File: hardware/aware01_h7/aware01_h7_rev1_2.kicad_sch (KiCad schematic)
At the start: 60 parts, among them J1 Conn_01x06_Pin, J2 Conn_01x03_Pin, SW1 SW_Push, U1 STM32H7B0ZBTx, U2 IS45S16800F-7TLA2, Y1 WE-XTAL 24.0MHz 50ppm

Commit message: update to rev 1.2
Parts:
- C1, C2: Manufacturer_Name KEMET -> KEMET
- C14, C7: Manufacturer_Name Samsung Electro-Mechanics -> Samsung Electro-Mechanics
- R40, R41, R42, R43, R44, R45, R46, R47, R48, R49, R50, R51, R52, R53, R54, R55, R56, R57, R58, R59, R60, R61, R62, R63, R64, R65, R66, R67, R68, R69, R70, R71, R72, R73, R74, R75, R76, R77: value 10 -> 33; footprint (none) -> Resistor_SMD:R_0603_1608Metric_Pad0.98x0.95mm_HandSolder; Manufacturer_Name (none) -> Susumu; Manufacturer_Part_Number (none) -> RR0510R-330-D; Mouser Part Number (none) -> 754-RR0510R-330D
- SW1: Manufacturer_Part_Number TS04-66-43-BK-100-SMT -> TS04-66-43-BK-100-SMT
- U1: Manufacturer_Part_Number STM32H7B0ZBT6 -> STM32H7B0ZBT6; Mouser Part Number 511-STM32H7B0ZBT6 -> 511-STM32H7B0ZBT6
- U2: Manufacturer_Name ISSI -> ISSI; Mouser Part Number 870-IS45S16800F7TLA2 -> 870-IS45S16800F7TLA2
- Y1: Mouser Part Number 710-830064703 -> 710-830064703

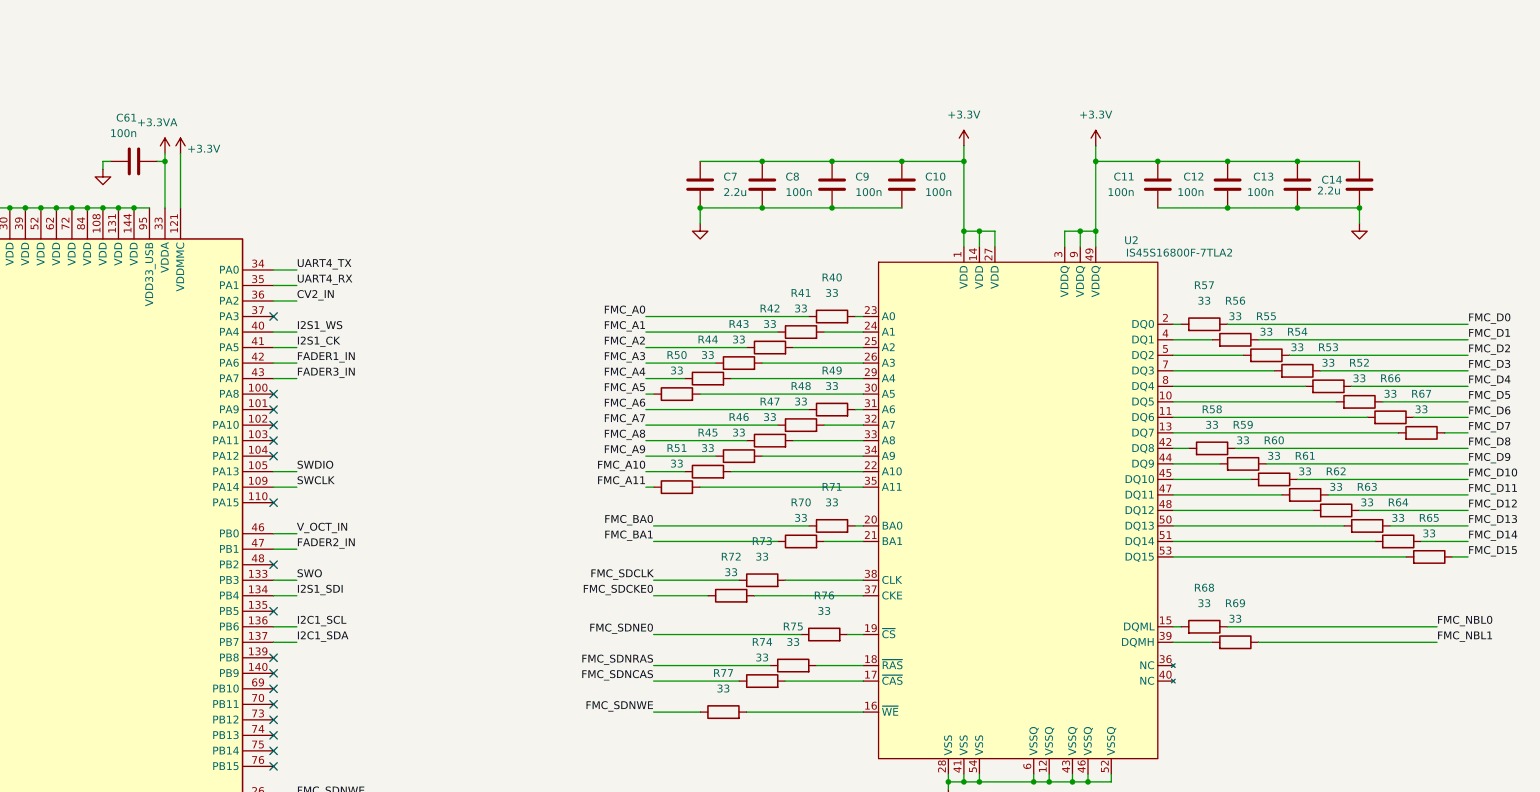
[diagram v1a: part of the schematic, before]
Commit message: rework layout and insert eletrolytic caps for gainstages
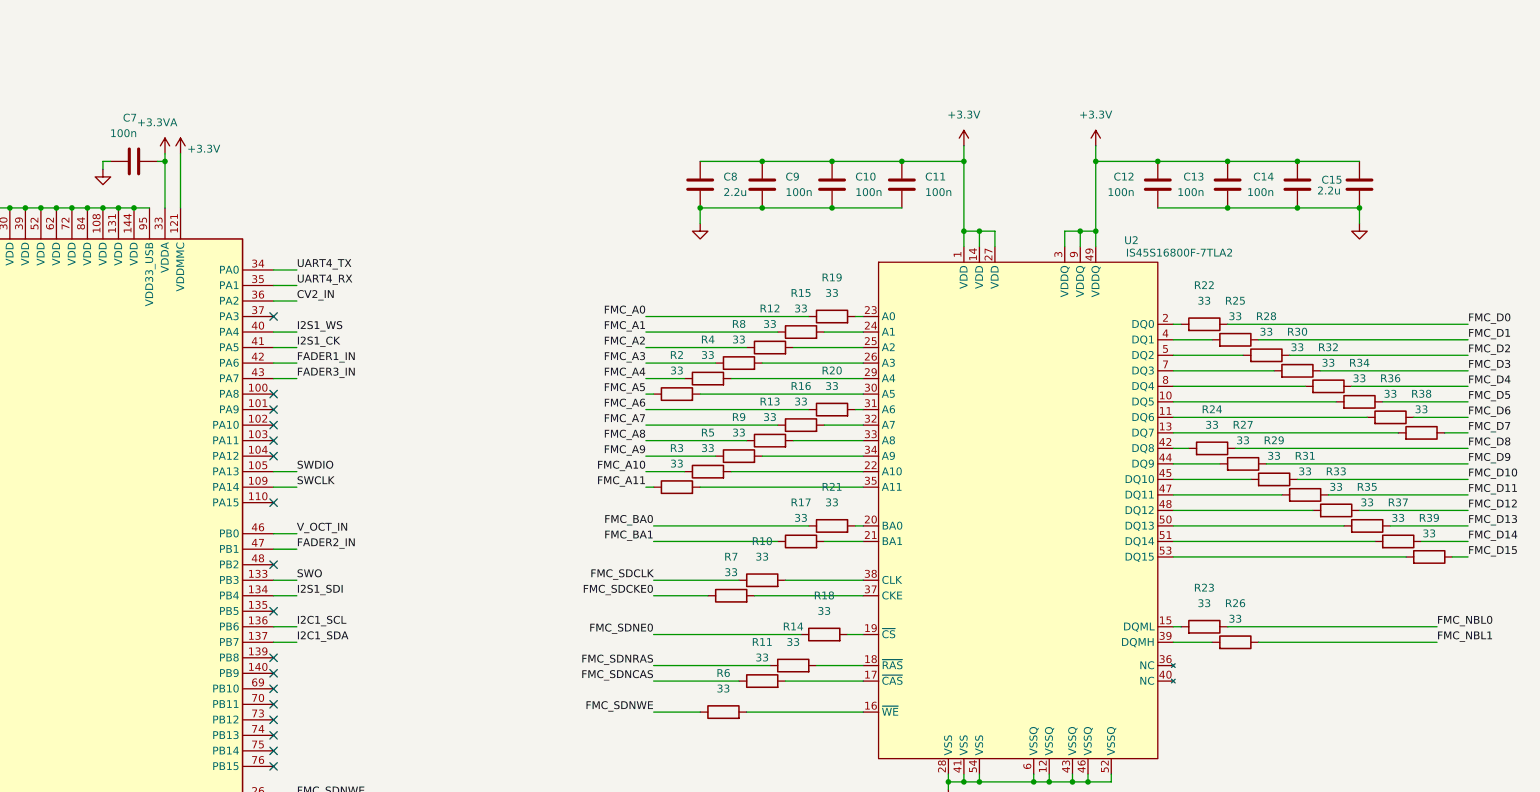
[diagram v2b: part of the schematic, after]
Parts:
- R10: renamed from R73; footprint Resistor_SMD:R_0603_1608Metric_Pad0.98x0.95mm_HandSolder -> Resistor_SMD:R_0402_1005Metric_Pad0.72x0.64mm_HandSolder
- R11: renamed from R74; footprint Resistor_SMD:R_0603_1608Metric_Pad0.98x0.95mm_HandSolder -> Resistor_SMD:R_0402_1005Metric_Pad0.72x0.64mm_HandSolder
- R12: renamed from R42; footprint Resistor_SMD:R_0603_1608Metric_Pad0.98x0.95mm_HandSolder -> Resistor_SMD:R_0402_1005Metric_Pad0.72x0.64mm_HandSolder
- R13: renamed from R47; footprint Resistor_SMD:R_0603_1608Metric_Pad0.98x0.95mm_HandSolder -> Resistor_SMD:R_0402_1005Metric_Pad0.72x0.64mm_HandSolder
- R14: renamed from R75; footprint Resistor_SMD:R_0603_1608Metric_Pad0.98x0.95mm_HandSolder -> Resistor_SMD:R_0402_1005Metric_Pad0.72x0.64mm_HandSolder
- R15: renamed from R41; footprint Resistor_SMD:R_0603_1608Metric_Pad0.98x0.95mm_HandSolder -> Resistor_SMD:R_0402_1005Metric_Pad0.72x0.64mm_HandSolder
- R16: renamed from R48; footprint Resistor_SMD:R_0603_1608Metric_Pad0.98x0.95mm_HandSolder -> Resistor_SMD:R_0402_1005Metric_Pad0.72x0.64mm_HandSolder
- R17: renamed from R70; footprint Resistor_SMD:R_0603_1608Metric_Pad0.98x0.95mm_HandSolder -> Resistor_SMD:R_0402_1005Metric_Pad0.72x0.64mm_HandSolder
- R18: renamed from R76; footprint Resistor_SMD:R_0603_1608Metric_Pad0.98x0.95mm_HandSolder -> Resistor_SMD:R_0402_1005Metric_Pad0.72x0.64mm_HandSolder
- R19: renamed from R40; footprint Resistor_SMD:R_0603_1608Metric_Pad0.98x0.95mm_HandSolder -> Resistor_SMD:R_0402_1005Metric_Pad0.72x0.64mm_HandSolder
- R2: renamed from R50; footprint Resistor_SMD:R_0603_1608Metric_Pad0.98x0.95mm_HandSolder -> Resistor_SMD:R_0402_1005Metric_Pad0.72x0.64mm_HandSolder
- R20: renamed from R49; footprint Resistor_SMD:R_0603_1608Metric_Pad0.98x0.95mm_HandSolder -> Resistor_SMD:R_0402_1005Metric_Pad0.72x0.64mm_HandSolder
- R21: renamed from R71; footprint Resistor_SMD:R_0603_1608Metric_Pad0.98x0.95mm_HandSolder -> Resistor_SMD:R_0402_1005Metric_Pad0.72x0.64mm_HandSolder
- R22: renamed from R57; footprint Resistor_SMD:R_0603_1608Metric_Pad0.98x0.95mm_HandSolder -> Resistor_SMD:R_0402_1005Metric_Pad0.72x0.64mm_HandSolder
- R23: renamed from R68; footprint Resistor_SMD:R_0603_1608Metric_Pad0.98x0.95mm_HandSolder -> Resistor_SMD:R_0402_1005Metric_Pad0.72x0.64mm_HandSolder
- R24: renamed from R58; footprint Resistor_SMD:R_0603_1608Metric_Pad0.98x0.95mm_HandSolder -> Resistor_SMD:R_0402_1005Metric_Pad0.72x0.64mm_HandSolder
- R25: renamed from R56; footprint Resistor_SMD:R_0603_1608Metric_Pad0.98x0.95mm_HandSolder -> Resistor_SMD:R_0402_1005Metric_Pad0.72x0.64mm_HandSolder
- R26: renamed from R69; footprint Resistor_SMD:R_0603_1608Metric_Pad0.98x0.95mm_HandSolder -> Resistor_SMD:R_0402_1005Metric_Pad0.72x0.64mm_HandSolder
- R27: renamed from R59; footprint Resistor_SMD:R_0603_1608Metric_Pad0.98x0.95mm_HandSolder -> Resistor_SMD:R_0402_1005Metric_Pad0.72x0.64mm_HandSolder
- R28: renamed from R55; footprint Resistor_SMD:R_0603_1608Metric_Pad0.98x0.95mm_HandSolder -> Resistor_SMD:R_0402_1005Metric_Pad0.72x0.64mm_HandSolder
- R29: renamed from R60; footprint Resistor_SMD:R_0603_1608Metric_Pad0.98x0.95mm_HandSolder -> Resistor_SMD:R_0402_1005Metric_Pad0.72x0.64mm_HandSolder
- R3: renamed from R51; footprint Resistor_SMD:R_0603_1608Metric_Pad0.98x0.95mm_HandSolder -> Resistor_SMD:R_0402_1005Metric_Pad0.72x0.64mm_HandSolder
- R30: renamed from R54; footprint Resistor_SMD:R_0603_1608Metric_Pad0.98x0.95mm_HandSolder -> Resistor_SMD:R_0402_1005Metric_Pad0.72x0.64mm_HandSolder
- R31: renamed from R61; footprint Resistor_SMD:R_0603_1608Metric_Pad0.98x0.95mm_HandSolder -> Resistor_SMD:R_0402_1005Metric_Pad0.72x0.64mm_HandSolder
- R32: renamed from R53; footprint Resistor_SMD:R_0603_1608Metric_Pad0.98x0.95mm_HandSolder -> Resistor_SMD:R_0402_1005Metric_Pad0.72x0.64mm_HandSolder
- R33: renamed from R62; footprint Resistor_SMD:R_0603_1608Metric_Pad0.98x0.95mm_HandSolder -> Resistor_SMD:R_0402_1005Metric_Pad0.72x0.64mm_HandSolder
- R34: renamed from R52; footprint Resistor_SMD:R_0603_1608Metric_Pad0.98x0.95mm_HandSolder -> Resistor_SMD:R_0402_1005Metric_Pad0.72x0.64mm_HandSolder
- R35: renamed from R63; footprint Resistor_SMD:R_0603_1608Metric_Pad0.98x0.95mm_HandSolder -> Resistor_SMD:R_0402_1005Metric_Pad0.72x0.64mm_HandSolder
- R36: renamed from R66; footprint Resistor_SMD:R_0603_1608Metric_Pad0.98x0.95mm_HandSolder -> Resistor_SMD:R_0402_1005Metric_Pad0.72x0.64mm_HandSolder
- R37: renamed from R64; footprint Resistor_SMD:R_0603_1608Metric_Pad0.98x0.95mm_HandSolder -> Resistor_SMD:R_0402_1005Metric_Pad0.72x0.64mm_HandSolder
- R38: renamed from R67; footprint Resistor_SMD:R_0603_1608Metric_Pad0.98x0.95mm_HandSolder -> Resistor_SMD:R_0402_1005Metric_Pad0.72x0.64mm_HandSolder
- R39: renamed from R65; footprint Resistor_SMD:R_0603_1608Metric_Pad0.98x0.95mm_HandSolder -> Resistor_SMD:R_0402_1005Metric_Pad0.72x0.64mm_HandSolder
- R4: renamed from R44; footprint Resistor_SMD:R_0603_1608Metric_Pad0.98x0.95mm_HandSolder -> Resistor_SMD:R_0402_1005Metric_Pad0.72x0.64mm_HandSolder
- R5: renamed from R45; footprint Resistor_SMD:R_0603_1608Metric_Pad0.98x0.95mm_HandSolder -> Resistor_SMD:R_0402_1005Metric_Pad0.72x0.64mm_HandSolder
- R6: renamed from R77; footprint Resistor_SMD:R_0603_1608Metric_Pad0.98x0.95mm_HandSolder -> Resistor_SMD:R_0402_1005Metric_Pad0.72x0.64mm_HandSolder
- R7: renamed from R72; footprint Resistor_SMD:R_0603_1608Metric_Pad0.98x0.95mm_HandSolder -> Resistor_SMD:R_0402_1005Metric_Pad0.72x0.64mm_HandSolder
- R8: renamed from R43; footprint Resistor_SMD:R_0603_1608Metric_Pad0.98x0.95mm_HandSolder -> Resistor_SMD:R_0402_1005Metric_Pad0.72x0.64mm_HandSolder
- R9: renamed from R46; footprint Resistor_SMD:R_0603_1608Metric_Pad0.98x0.95mm_HandSolder -> Resistor_SMD:R_0402_1005Metric_Pad0.72x0.64mm_HandSolder
- renumbered C9 to C10, C10 to C11, C11 to C12, C12 to C13, C13 to C14, C14 to C15, C61 to C7, C7 to C8, C8 to C9
